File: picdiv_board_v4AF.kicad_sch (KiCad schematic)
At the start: 56 parts, among them J1 DC-Input, J10 PPS_B, J11 PPS_B, J2 MountingHole_M2.5, J3 MountingHole_M2.5, J4 TEST_1PPS, J5 Conn_01x06, J6 Sync, J7 Sync, J8 10MHz, J9 10MHz, SW1 SW_DIP_x03, U1 LT1963AxST-3.3, U2 LT1963AxST-3.3, U3 PIC12F675-xSN, U4 LTC6993xS6-1, U5 IDT5PB1108, U6 IDT5PB1108

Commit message: Add .stp file for FL1
Added manufacturer .stp file for FL1.   The footprint is a kicad library part, so I made the change on the schematic.
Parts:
- J1: footprint Connectors_Terminal_Blocks:TerminalBlock_bornier-2_P5.08mm -> TerminalBlock_Phoenix:TerminalBlock_Phoenix_MKDS-1,5-2-5.08_1x02_P5.08mm_Horizontal
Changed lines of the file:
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@@
 			)
 		)
-		(property "Footprint" "Connectors_Terminal_Blocks:TerminalBlock_bornier-2_P5.08mm"
+		(property "Footprint" "TerminalBlock_Phoenix:TerminalBlock_Phoenix_MKDS-1,5-2-5.08_1x02_P5.08mm_Horizontal"
 			(at 20.32 163.83 0)
 			(effects

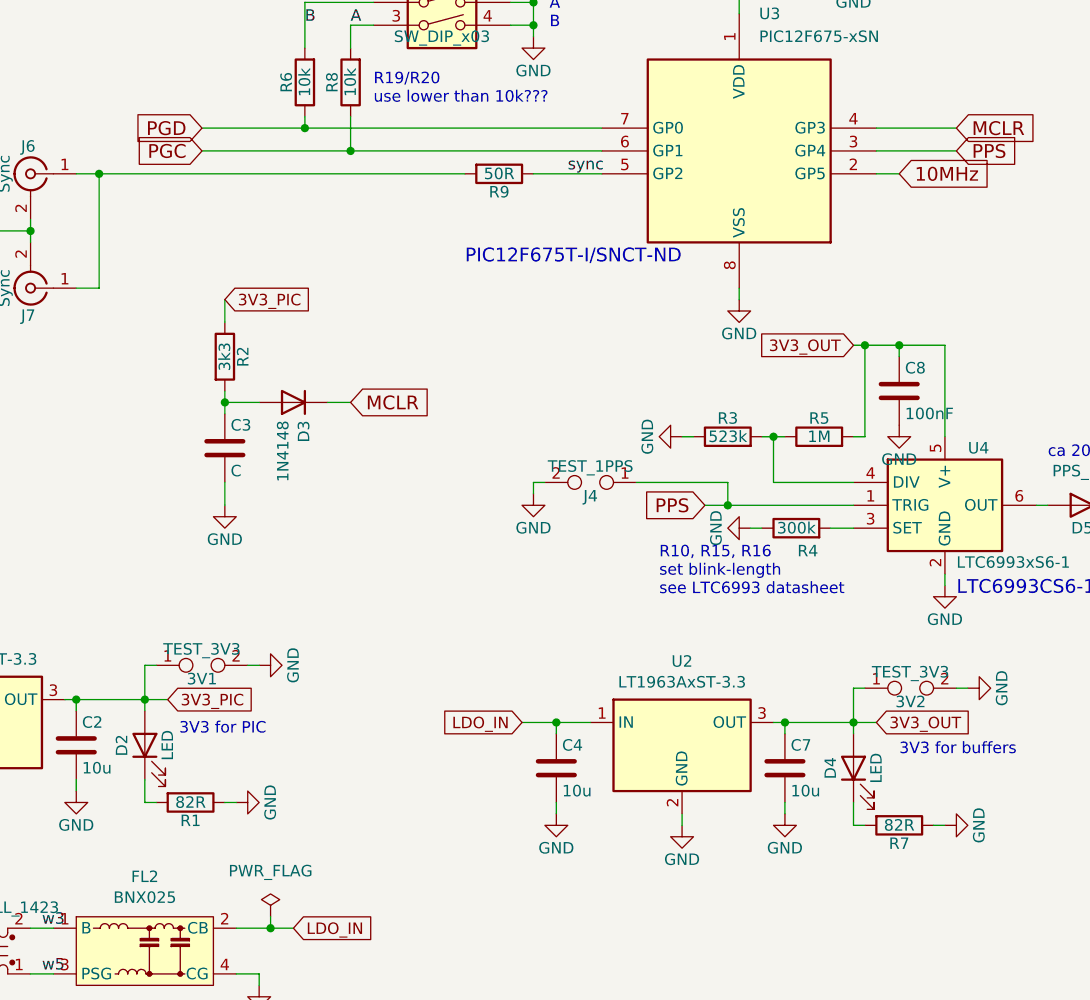
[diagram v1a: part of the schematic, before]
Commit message: Add LCSC numbers for some resistors.
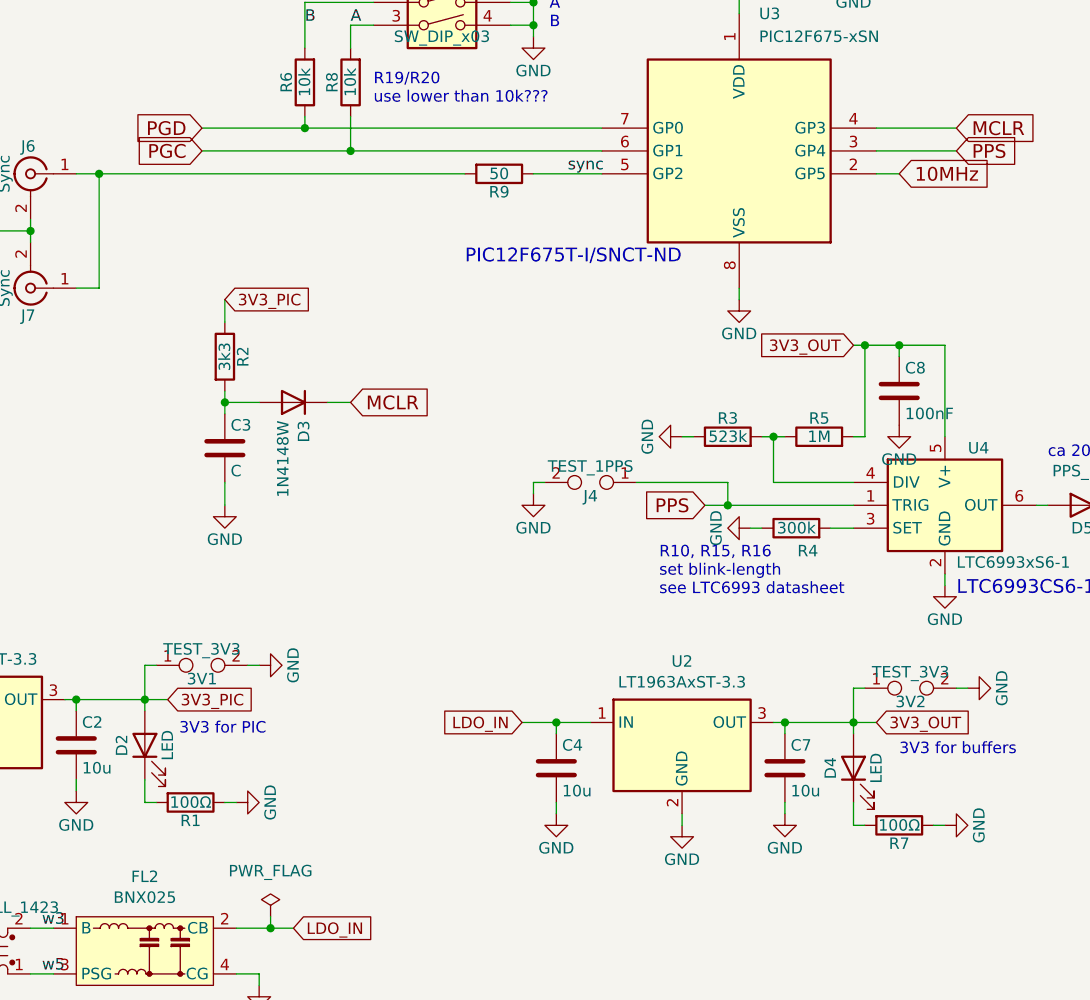
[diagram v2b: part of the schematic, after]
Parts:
- C2, C4, C5, C7: LCSC (none) -> C15850
- D3: value 1N4148 -> 1N4148W; LCSC (none) -> C81598
- R1: value 82R -> 100Ω; LCSC (none) -> C17408
- R7: value 82R -> 100Ω; LCSC (none) -> C17408; MPN (none) -> 0805W8F1000T5E
- R9: value 50R -> 50; LCSC (none) -> C2828865
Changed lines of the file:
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@@
 			)
 		)
-		(property "Description" "Unpolarized capacitor"
+		(property "Description" "25V X5R"
 			(at 140.97 50.8 0)
 			(effects
@@
 			)
 		)
-		(property "LCSC" ""
+		(property "LCSC" "C15850"
 			(at 140.97 50.8 0)
 			(effects
@@
 			)
 		)
-		(property "Value" "50R"
+		(property "Value" "50"
 			(at 101.6 80.01 90)
 			(effects
@@
 			)
 		)
-		(property "Description" "Resistor"
+		(property "Description" "Resistor 1%"
 			(at 101.6 80.01 0)
 			(effects
@@
 			)
 		)
+		(property "LCSC" "C2828865"
+			(at 101.6 80.01 90)
+			(effects
+				(font
+					(size 1.27 1.27)
+				)
+				(hide yes)
+			)
+		)
 		(pin "1"
 		)
@@
 			)
 		)
-		(property "Value" "1N4148"
+		(property "Value" "1N4148W"
 			(at 77.597 107.4166 90)
 			(effects
@@
 			)
 		)
+		(property "LCSC" "C81598"
+			(at 78.74 105.41 90)
+			(effects
+				(font
+					(size 1.27 1.27)
+				)
+				(hide yes)
+			)
+		)
 		(pin "1"
 		)
@@
 			)
 		)
-		(property "Description" "Unpolarized capacitor"
+		(property "Description" "25V X5R"
+			(at 54.61 143.51 0)
+			(effects
+				(font
+					(size 1.27 1.27)
+				)
+				(hide yes)
+			)
+		)
+		(property "MPN" ""
+			(at 54.61 143.51 0)
+			(effects
+				(font
+					(size 1.27 1.27)
+				)
+				(hide yes)
+			)
+		)
+		(property "LCSC" "C15850"
 			(at 54.61 143.51 0)
 			(effects
@@
 			)
 		)
-		(property "Value" "82R"
+		(property "Value" "100Ω"
 			(at 67.31 149.86 90)
 			(effects
@@
 			)
 		)
+		(property "MPN" ""
+			(at 67.31 149.86 90)
+			(effects
+				(font
+					(size 1.27 1.27)
+				)
+				(hide yes)
+			)
+		)
+		(property "LCSC" "C17408"
+			(at 67.31 149.86 90)
+			(effects
+				(font
+					(size 1.27 1.27)
+				)
+				(hide yes)
+			)
+		)
 		(pin "1"
 		)
@@
 			)
 		)
-		(property "Description" "Unpolarized capacitor"
+		(property "Description" "25V X5R"
+			(at 107.95 146.05 0)
+			(effects
+				(font
+					(size 1.27 1.27)
+				)
+				(hide yes)
+			)
+		)
+		(property "MPN" ""
+			(at 107.95 146.05 0)
+			(effects
+				(font
+					(size 1.27 1.27)
+				)
+				(hide yes)
+			)
+		)
+		(property "LCSC" "C15850"
 			(at 107.95 146.05 0)
 			(effects
@@
 			)
 		)
-		(property "Description" "Unpolarized capacitor"
+		(property "Description" "25V X5R"
+			(at 133.35 146.05 0)
+			(effects
+				(font
+					(size 1.27 1.27)
+				)
+				(hide yes)
+			)
+		)
+		(property "MPN" ""
+			(at 133.35 146.05 0)
+			(effects
+				(font
+					(size 1.27 1.27)
+				)
+				(hide yes)
+			)
+		)
+		(property "LCSC" "C15850"
 			(at 133.35 146.05 0)
 			(effects
@@
 			)
 		)
-		(property "Value" "82R"
+		(property "Value" "100Ω"
 			(at 146.05 152.4 90)
 			(effects
@@
 			(effects
 				(font
+					(size 1.27 1.27)
+				)
+				(hide yes)
+			)
+		)
+		(property "MPN" "0805W8F1000T5E"
+			(at 146.05 152.4 90)
+			(effects
+				(font
+					(size 1.27 1.27)
+				)
+				(hide yes)
+			)
+		)
+		(property "LCSC" "C17408 "
+			(at 146.05 152.4 90)
+			(effects
+				(font

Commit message: DC Input layout
Fix keep out area around DC Input.   Add vias to FL2 GND.   The vias used to be in the foot print, but are no longer there in the current version of KiCad.  Easier to keep the library part and add the vias.
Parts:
- C1: LCSC (none) -> C15850
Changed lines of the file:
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@@
 			)
 		)
-		(property "Description" "Unpolarized capacitor"
+		(property "Description" "25V X5R"
 			(at 29.21 143.51 0)
 			(effects
+				(font
+					(size 1.27 1.27)
+				)
+				(hide yes)
+			)
+		)
+		(property "MPN" ""
+			(at 29.21 143.51 0)
+			(effects
+				(font
+					(size 1.27 1.27)
+				)
+				(hide yes)
+			)
+		)
+		(property "LCSC" "C15850"
+			(at 29.21 143.51 0)
+			(effects

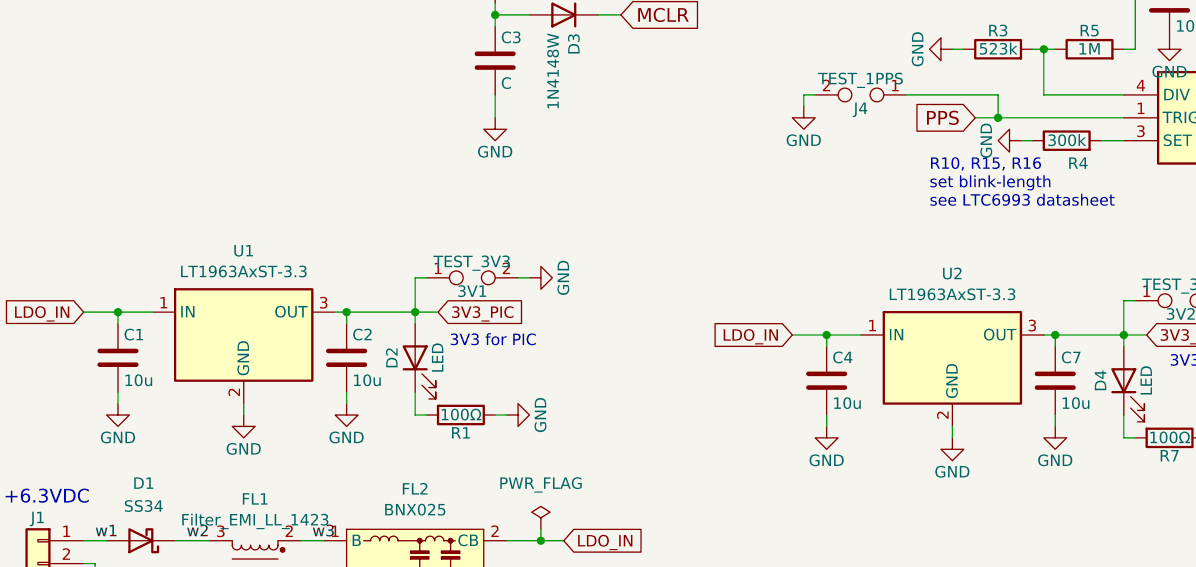
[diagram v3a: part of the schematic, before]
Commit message: Add LCSC      part numbers to schematic
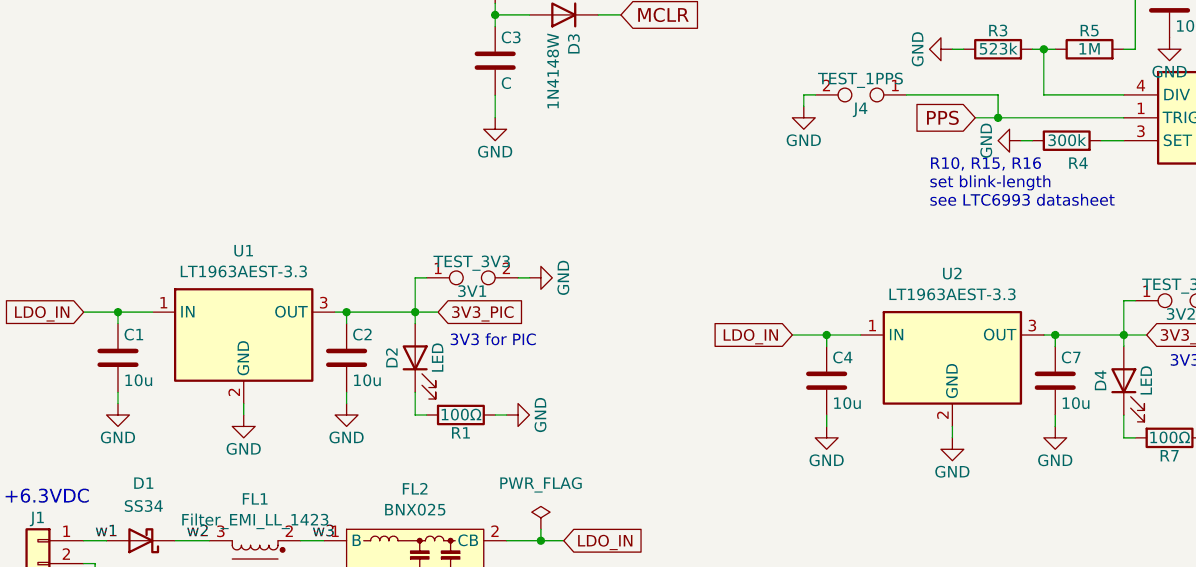
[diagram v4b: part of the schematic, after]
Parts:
- U1, U2: value LT1963AxST-3.3 -> LT1963AEST-3.3; LCSC (none) -> C459918
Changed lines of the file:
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@@
+			)
+		)
+		(property "Sim.Device" "R"
+			(at 67.31 149.86 0)
+			(effects
+				(font
+					(size 1.27 1.27)
+				)
+				(hide yes)
+			)
+		)
+		(property "Sim.Pins" "1=+ 2=-"
+			(at 67.31 149.86 0)
+			(effects
+				(font
+					(size 1.27 1.27)
+				)
+				(hide yes)
+			)
+		)
+		(property "Sim.Params" "r=\"\""
+			(at 67.31 149.86 0)
+			(effects
+				(font
+					(size 1.27 1.27)
+				)
+				(hide yes)
 			)
 		)
@@
 			)
 		)
+		(property "Sim.Device" "R"
+			(at 146.05 152.4 0)
+			(effects
+				(font
+					(size 1.27 1.27)
+				)
+				(hide yes)
+			)
+		)
+		(property "Sim.Pins" "1=+ 2=-"
+			(at 146.05 152.4 0)
+			(effects
+				(font
+					(size 1.27 1.27)
+				)
+				(hide yes)
+			)
+		)
+		(property "Sim.Params" "r=\"\""
+			(at 146.05 152.4 0)
+			(effects
+				(font
+					(size 1.27 1.27)
+				)
+				(hide yes)
+			)
+		)
 		(pin "1"
 		)
@@
 			)
 		)
-		(property "Value" "LT1963AxST-3.3"
+		(property "Value" "LT1963AEST-3.3"
 			(at 121.92 136.4996 0)
 			(effects
@@
 			)
 		)
+		(property "LCSC" "C459918"
+			(at 121.92 143.51 0)
+			(effects
+				(font
+					(size 1.27 1.27)
+				)
+				(hide yes)
+			)
+		)
 		(pin "1"
 		)
@@
 			)
 		)
-		(property "Value" "LT1963AxST-3.3"
+		(property "Value" "LT1963AEST-3.3"
 			(at 43.18 133.9596 0)
 			(effects
@@
 			(at 43.18 140.97 0)
 			(effects
+				(font
+					(size 1.27 1.27)
+				)
+				(hide yes)
+			)
+		)
+		(property "LCSC" "C459918"
+			(at 43.18 140.97 0)
+			(effects

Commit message: More layout, mostly around Vadg
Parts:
- D2: LCSC (none) -> C2297; MPN (none) -> KT-0805G
- D4: LCSC (none) -> C2297
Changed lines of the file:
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@@
 			)
 		)
-		(property "Description" "Light emitting diode"
+		(property "Description" "Green LED 0805"
+			(at 62.23 143.51 0)
+			(effects
+				(font
+					(size 1.27 1.27)
+				)
+				(hide yes)
+			)
+		)
+		(property "MPN" "KT-0805G"
+			(at 62.23 143.51 0)
+			(effects
+				(font
+					(size 1.27 1.27)
+				)
+				(hide yes)
+			)
+		)
+		(property "LCSC" "C2297 "
 			(at 62.23 143.51 0)
 			(effects
@@
 			)
 		)
-		(property "Description" "Light emitting diode"
+		(property "Description" "Green LED 0805"
 			(at 140.97 146.05 0)
 			(effects
+				(font
+					(size 1.27 1.27)
+				)
+				(hide yes)
+			)
+		)
+		(property "MPN" ""
+			(at 140.97 146.05 0)
+			(effects
+				(font
+					(size 1.27 1.27)
+				)
+				(hide yes)
+			)
+		)
+		(property "LCSC" "C2297"
+			(at 140.97 146.05 0)
+			(effects

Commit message: More layout
Vadj getting closer.   Keep out around OCXO
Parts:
- L1, L2, L3: LCSC (none) -> C1043; MPN (none) -> CMI201209U2R2KT
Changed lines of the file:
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@@
 			)
 		)
-		(property "Description" "Inductor"
+		(property "Description" "50mA 2.2uH ±10% 600mΩ"
 			(at 116.84 44.45 0)
 			(effects
@@
 			)
 		)
+		(property "MPN" "CMI201209U2R2KT"
+			(at 116.84 44.45 90)
+			(effects
+				(font
+					(size 1.27 1.27)
+				)
+				(hide yes)
+			)
+		)
+		(property "LCSC" "C1043"
+			(at 116.84 44.45 90)
+			(effects
+				(font
+					(size 1.27 1.27)
+				)
+				(hide yes)
+			)
+		)
 		(pin "1"
 		)
@@
 			)
 		)
+		(property "MPN" "CMI201209U2R2KT"
+			(at 223.52 80.01 90)
+			(effects
+				(font
+					(size 1.27 1.27)
+				)
+				(hide yes)
+			)
+		)
+		(property "LCSC" "C1043"
+			(at 223.52 80.01 90)
+			(effects
+				(font
+					(size 1.27 1.27)
+				)
+				(hide yes)
+			)
+		)
 		(pin "1"
 		)
@@
 			(effects
 				(font
+					(size 1.27 1.27)
+				)
+				(hide yes)
+			)
+		)
+		(property "MPN" "CMI201209U2R2KT"
+			(at 223.52 27.94 90)
+			(effects
+				(font
+					(size 1.27 1.27)
+				)
+				(hide yes)
+			)
+		)
+		(property "LCSC" "C1043"
+			(at 223.52 27.94 90)
+			(effects
+				(font

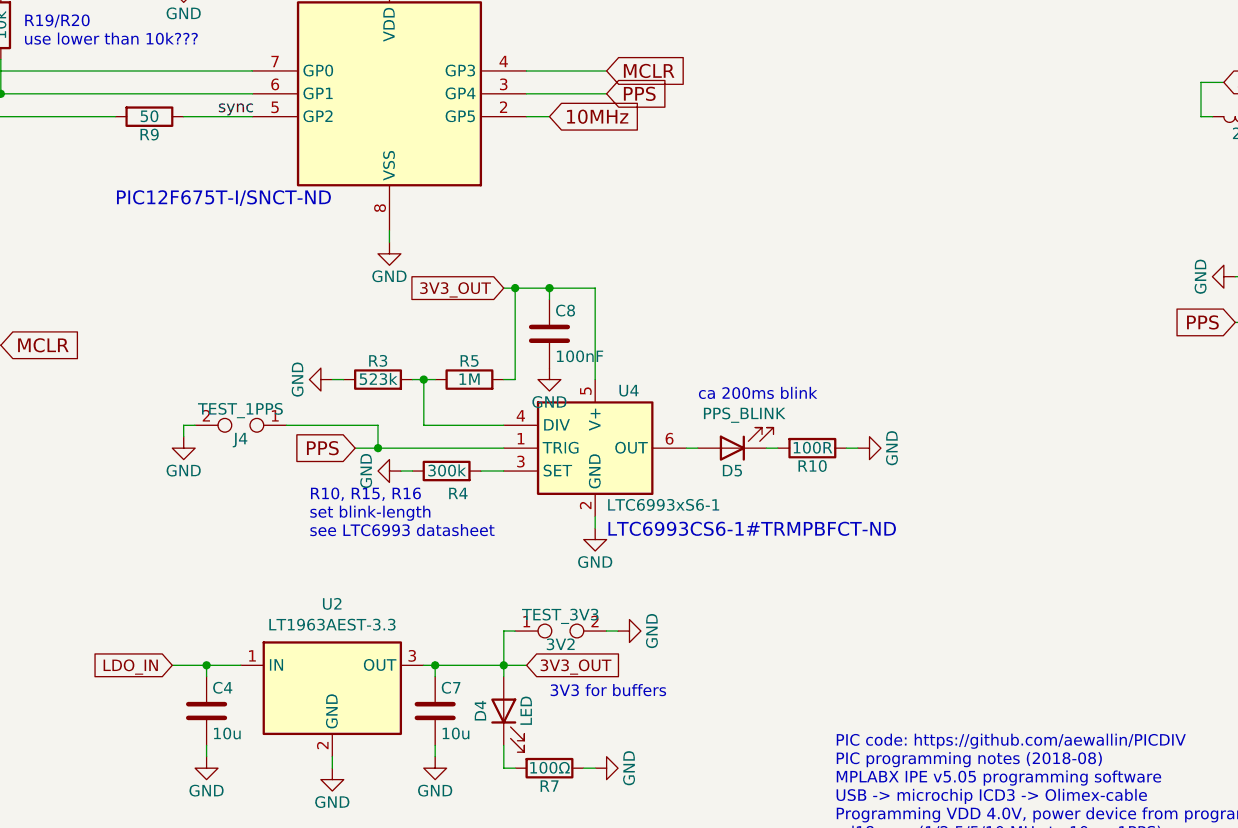
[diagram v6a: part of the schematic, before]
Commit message: Led Blink
Replace pricey LT monostable with an NE555.  No need for an expensive part.
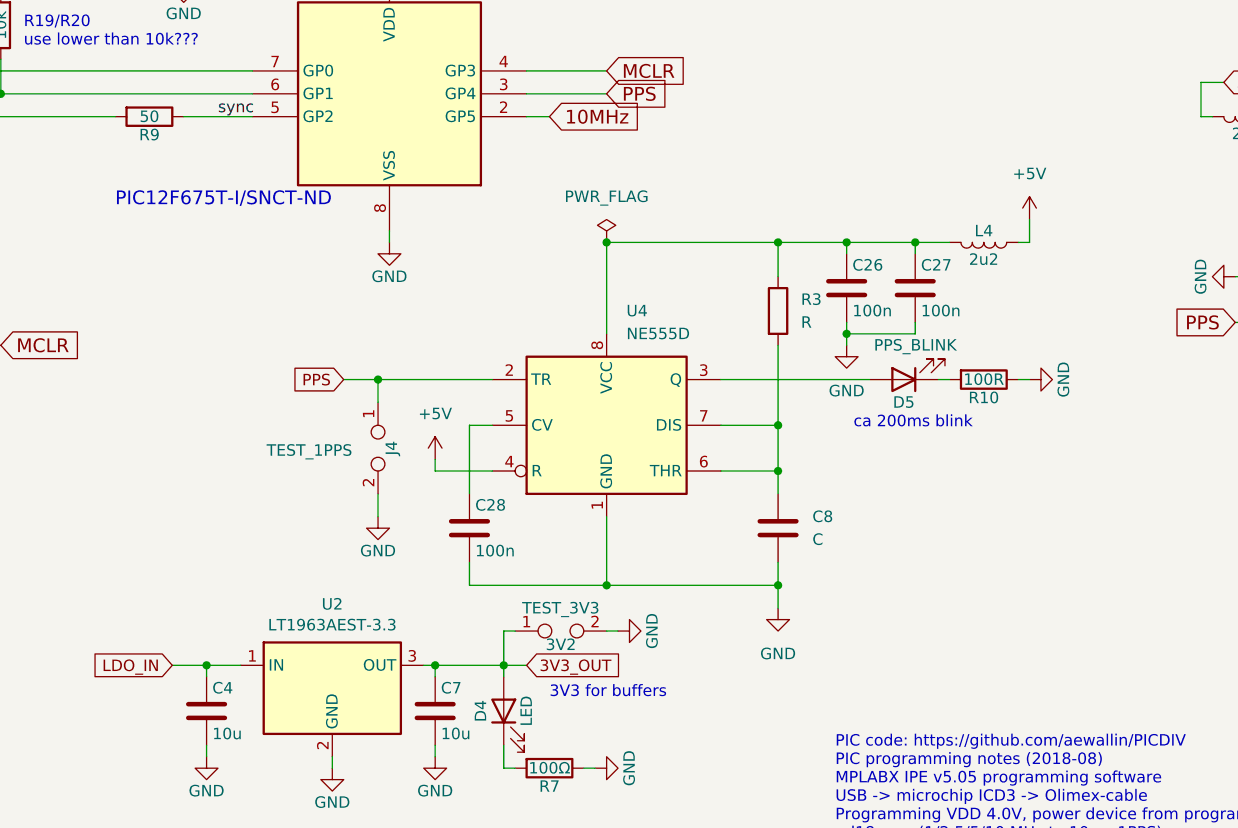
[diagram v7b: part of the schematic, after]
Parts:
- removed R4: 300k, Resistor_SMD:R_0805_2012Metric, symbol Device:R
- removed R5: 1M, Resistor_SMD:R_0805_2012Metric, symbol Device:R
- removed U4: LTC6993xS6-1, Package_TO_SOT_SMD:TSOT-23-6, symbol Timer:LTC6993xS6-1
- added C26, C27, C28: 100n, Capacitor_SMD:C_0805_2012Metric, symbol Device:C
- added L4: 2u2, Inductor_SMD:L_0805_2012Metric, symbol Device:L
- added U4: NE555D, Package_SO:SOIC-8_3.9x4.9mm_P1.27mm, symbol Timer:NE555D
- C8: value 100nF -> C; LCSC C49678 -> (none); MPN CC0805KRX7R9BB104 -> (none)
- R3: value 523k -> R
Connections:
- net 3V3_OUT: no longer C8.1
- net GND: now also C26.2, C27.2, C28.2, U4.1 (GND); no longer R3.1
- net PPS: now also U4.2 (TR)
- net at D5.2 (A): now also U4.3 (Q)
- net at R3.2: now also C8.1, U4.6 (THR), U4.7 (DIS)
- new net: C28.1, U4.5 (CV)
- new net: C26.1, C27.1, L4.2, R3.1, U4.8 (VCC)
- new net +5V: L4.1, U4.4 (R)
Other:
- note removed: "LTC6993CS6-1#TRMPBFCT-ND"
- note removed: "R10, R15, R16 set blink-length see LTC6993 datasheet"
- moved on the sheet: D5, J4, R10

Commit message: 555 work
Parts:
- C8: value C -> 1µF; LCSC (none) -> C28323; MPN (none) -> CL21B105KBFNNNE
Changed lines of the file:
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@@
 			)
 		)
-		(property "Value" "C"
+		(property "Value" "1µF"
 			(at 175.26 126.9999 0)
 			(effects
@@
 			)
 		)
-		(property "Description" "Unpolarized capacitor"
+		(property "Description" "50V X7R, Basic Part"
 			(at 171.45 125.73 0)
 			(effects
+				(font
+					(size 1.27 1.27)
+				)
+				(hide yes)
+			)
+		)
+		(property "MPN" "CL21B105KBFNNNE"
+			(at 171.45 125.73 0)
+			(effects
+				(font
+					(size 1.27 1.27)
+				)
+				(hide yes)
+			)
+		)
+		(property "LCSC" "C28323"
+			(at 171.45 125.73 0)
+			(effects
